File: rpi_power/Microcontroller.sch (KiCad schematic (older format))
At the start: 12 parts, among them U2 ATxmega16A4U-AU, U3 LM2936-3.3, Y1 Crystal

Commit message: Components placed.
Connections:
- net ADC0: now also U2.28 (PE0); no longer U2.40 (AREFA/PA0)
- net ADC1: now also U2.29 (PE1); no longer U2.41 (PA1)
- net ADC2: now also U2.32 (PE2); no longer U2.42 (PA2)
- net ADC3: now also U2.33 (PE3); no longer U2.43 (PA3)
- net ENABLE: now also U2.7 (PB3); no longer U2.33 (PE3)
- net GPIO0: now also U2.23 (PD3); no longer U2.20 (PD0)
- net GPIO1: now also U2.24 (PD4); no longer U2.21 (PD1)
- net GPIO2: now also U2.25 (PD5); no longer U2.22 (PD2)
- net GPIO3: now also U2.26 (PD6); no longer U2.23 (PD3)
- net GPIO4: now also U2.27 (PD7); no longer U2.24 (PD4)
- net POWER_STATE: now also U2.6 (PB2); no longer U2.32 (PE2)
- net VCOND_MEASURE: now also U2.4 (AREFB/PB0); no longer U2.28 (PE0)
- net WATCHDOG: now also U2.5 (PB1); no longer U2.29 (PE1)
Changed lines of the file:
@@
 Wire Wire Line
 	4650 3850 4800 3850
-Wire Wire Line
-	4650 2350 4800 2350
-Wire Wire Line
-	4650 2450 4800 2450
-Wire Wire Line
-	4650 2550 4800 2550
-Wire Wire Line
-	4650 2650 4800 2650
-Wire Wire Line
-	3250 3250 3100 3250
-Wire Wire Line
-	3250 3350 3100 3350
-Wire Wire Line
-	3250 3450 3100 3450
-Wire Wire Line
-	3250 3550 3100 3550
-Text GLabel 3100 3550 0    50   Output ~ 0
+Text GLabel 4650 3550 2    50   Output ~ 0
 ENABLE
-Text GLabel 3100 3250 0    50   Output ~ 0
+Text GLabel 4650 3250 2    50   Output ~ 0
 VCOND_MEASURE
-Text GLabel 3100 3450 0    50   Input ~ 0
+Text GLabel 4650 3450 2    50   Input ~ 0
 POWER_STATE
-Text GLabel 3100 3350 0    50   Input ~ 0
+Text GLabel 4650 3350 2    50   Input ~ 0
 WATCHDOG
-Text GLabel 4800 2350 2    50   Input ~ 0
+Text GLabel 3250 3250 0    50   Input ~ 0
 ADC0
-Text GLabel 4800 2450 2    50   Input ~ 0
+Text GLabel 3250 3350 0    50   Input ~ 0
 ADC1
-Text GLabel 4800 2550 2    50   Input ~ 0
+Text GLabel 3250 3450 0    50   Input ~ 0
 ADC2
-Text GLabel 4800 2650 2    50   Input ~ 0
+Text GLabel 3250 3550 0    50   Input ~ 0
 ADC3
 Text GLabel 4800 3750 2    50   BiDi ~ 0
@@
 Wire Wire Line
 	4200 1400 4400 1400
-Wire Wire Line
-	3150 3750 3250 3750
-Wire Wire Line
-	3150 3850 3250 3850
-Wire Wire Line
-	3150 3950 3250 3950
-Wire Wire Line
-	3150 4050 3250 4050
-Wire Wire Line
-	3150 4150 3250 4150
 NoConn ~ 4650 2750
 NoConn ~ 4650 2850
 NoConn ~ 4650 2950
 NoConn ~ 4650 3050
-NoConn ~ 4650 3250
-NoConn ~ 4650 3350
-NoConn ~ 4650 3450
-NoConn ~ 4650 3550
 NoConn ~ 4650 3950
 NoConn ~ 4650 4050
@@
 Text GLabel 3050 2200 1    50   Input ~ 0
 PDI_CLK
-Text GLabel 3150 3750 0    50   BiDi ~ 0
+Text GLabel 3250 4050 0    50   BiDi ~ 0
 GPIO0
-Text GLabel 3150 3850 0    50   BiDi ~ 0
+Text GLabel 3250 4150 0    50   BiDi ~ 0
 GPIO1
-Text GLabel 3150 3950 0    50   BiDi ~ 0
+Text GLabel 3250 4250 0    50   BiDi ~ 0
 GPIO2
-Text GLabel 3150 4050 0    50   BiDi ~ 0
+Text GLabel 3250 4350 0    50   BiDi ~ 0
 GPIO3
-Text GLabel 3150 4150 0    50   BiDi ~ 0
+Text GLabel 3250 4450 0    50   BiDi ~ 0
 GPIO4
-NoConn ~ 3250 4250
-NoConn ~ 3250 4350
-NoConn ~ 3250 4450
+NoConn ~ 3250 3750
+NoConn ~ 3250 3850
+NoConn ~ 3250 3950
+NoConn ~ 4650 2350
+NoConn ~ 4650 2450
+NoConn ~ 4650 2550
+NoConn ~ 4650 2650
 $EndSCHEMATC

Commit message: Updated some footprints.
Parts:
- C25: footprint Capacitor_Tantalum_SMD:CP_EIA-3216-10_Kemet-I_Pad1.58x1.35mm_HandSolder -> Capacitors:Tantalum_SMD_3216_KEMET_T491_HandSolder
- Y1: footprint Crystal:Crystal_SMD_Abracon_ABM3-2Pin_5.0x3.2mm_HandSoldering -> Crystals:Crystal_SMD_Abracon_ABM3-2Pin_5.0x3.2mm
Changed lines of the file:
@@
 F 0 "C25" H 9768 4596 50  0000 L CNN
 F 1 "22uF/6.3V" H 9768 4505 50  0000 L CNN
-F 2 "Capacitor_Tantalum_SMD:CP_EIA-3216-10_Kemet-I_Pad1.58x1.35mm_HandSolder" H 9688 4400 50  0001 C CNN
+F 2 "Capacitors:Tantalum_SMD_3216_KEMET_T491_HandSolder" H 9688 4400 50  0001 C CNN
 F 3 "~" H 9650 4550 50  0001 C CNN
 F 4 "2321204" H 350 1150 50  0001 C CNN "Farnell"
@@
 F 0 "Y1" H 1500 3200 50  0000 C CNN
 F 1 "Crystal" H 1500 3077 50  0000 C CNN
-F 2 "Crystal:Crystal_SMD_Abracon_ABM3-2Pin_5.0x3.2mm_HandSoldering" H 1500 2900 50  0001 C CNN
+F 2 "Crystals:Crystal_SMD_Abracon_ABM3-2Pin_5.0x3.2mm" H 1500 2900 50  0001 C CNN
 F 3 "~" H 1500 2900 50  0001 C CNN
 F 4 "2467791" H 1500 2900 50  0001 C CNN "Farnell"

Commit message: Routing done, pending review.
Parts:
- U3: symbol Regulator_Linear:LM2936-3.3 -> power_custom:LM2936-3.3; Farnell (none) -> 1469062
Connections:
- net ENABLE: now also U2.5 (PB1); no longer U2.7 (PB3)
- net GND: now also U3.4
- net WATCHDOG: now also U2.7 (PB3); no longer U2.5 (PB1)
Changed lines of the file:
@@
 $EndDescr
-$Comp
-L Regulator_Linear:LM2936-3.3 U3
-U 1 1 5BE4474B
-P 9100 4350
-F 0 "U3" H 9100 4592 50  0000 C CNN
-F 1 "LM2936-3.3" H 9100 4501 50  0000 C CNN
-F 2 "Package_TO_SOT_SMD:SOT-223" H 9100 4575 50  0001 C CIN
-F 3 "http://www.ti.com/lit/ds/symlink/lm2936.pdf" H 9100 4300 50  0001 C CNN
-F 4 "LM2936MP-3.3/NOPB" H 9100 4350 50  0001 C CNN "Ref"
-	1    9100 4350
-	1    0    0    -1
-$EndComp
 $Comp
 L power:GND #PWR050
@@
 Wire Wire Line
 	4650 3850 4800 3850
-Text GLabel 4650 3550 2    50   Output ~ 0
+Text GLabel 4650 3350 2    50   Output ~ 0
 ENABLE
 Text GLabel 4650 3250 2    50   Output ~ 0
@@
 Text GLabel 4650 3450 2    50   Input ~ 0
 POWER_STATE
-Text GLabel 4650 3350 2    50   Input ~ 0
+Text GLabel 4650 3550 2    50   Input ~ 0
 WATCHDOG
 Text GLabel 3250 3250 0    50   Input ~ 0
@@
 NoConn ~ 4650 2550
 NoConn ~ 4650 2650
+$Comp
+L power_custom:LM2936-3.3 U3
+U 1 1 5BE4474B
+P 9100 4350
+F 0 "U3" H 9100 4592 50  0000 C CNN
+F 1 "LM2936-3.3" H 9100 4501 50  0000 C CNN
+F 2 "Package_TO_SOT_SMD:SOT-223" H 9100 4575 50  0001 C CIN
+F 3 "http://www.ti.com/lit/ds/symlink/lm2936.pdf" H 9100 4300 50  0001 C CNN
+F 4 "1469062" H 9100 4350 50  0001 C CNN "Farnell"
+F 5 "LM2936MP-3.3/NOPB" H 9100 4350 50  0001 C CNN "Ref"
+	1    9100 4350
+	1    0    0    -1
+$EndComp
 $EndSCHEMATC

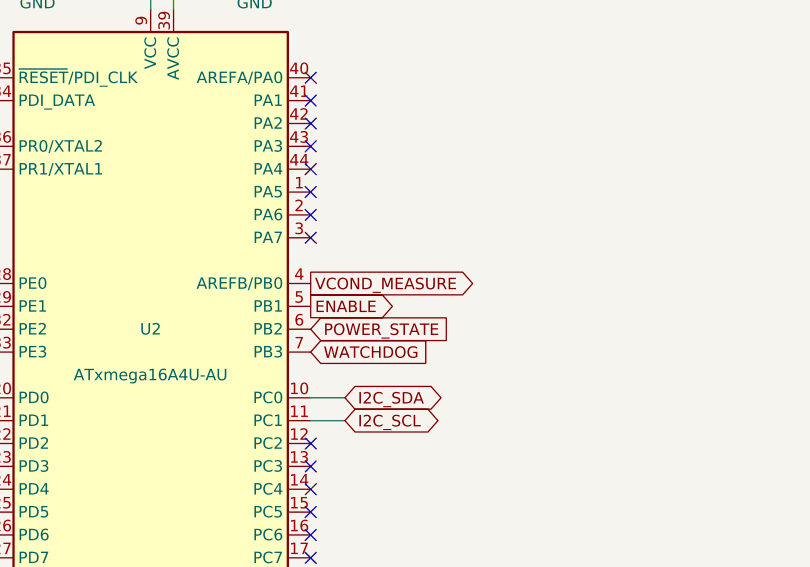
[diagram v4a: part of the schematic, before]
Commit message: Differentiated VCOND and BATT+. Routing done.
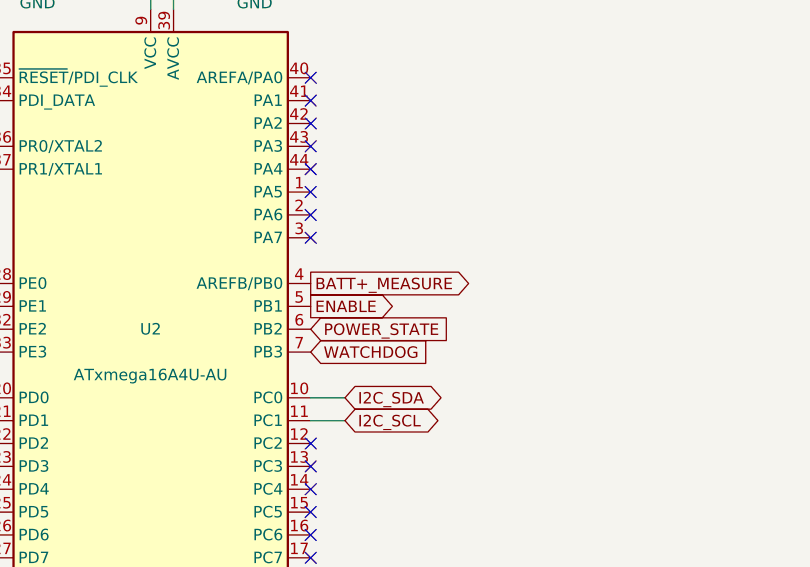
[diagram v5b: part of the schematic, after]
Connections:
- net VCOND_MEASURE renamed BATT+_MEASURE
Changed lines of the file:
@@
 ENABLE
 Text GLabel 4650 3250 2    50   Output ~ 0
-VCOND_MEASURE
+BATT+_MEASURE
 Text GLabel 4650 3450 2    50   Input ~ 0
 POWER_STATE
